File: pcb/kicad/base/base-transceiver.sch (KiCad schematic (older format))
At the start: 4 parts, among them U2 XBee-PRO_900HP

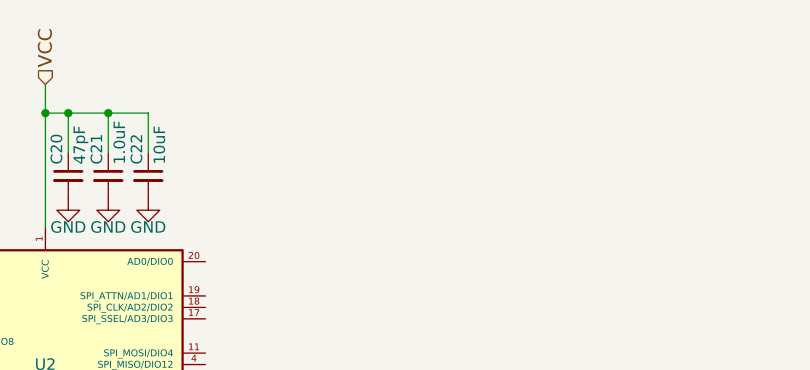
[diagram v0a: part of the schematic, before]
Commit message: Add initial layout for base daughterboard
Started the initial layout of the daughterboard with the
microcontroller. The inductors and crystals have placeholder footprints,
while the antenna and ferrite bead are TBD. Currently using default SMD
0402 size, but compact layout is still difficult to achieve. Crystals
have been placed as close as possible to the oscillator pins, but ground
return path is not optimized. Extent of components to be placed on
daughterboard still not finalized.
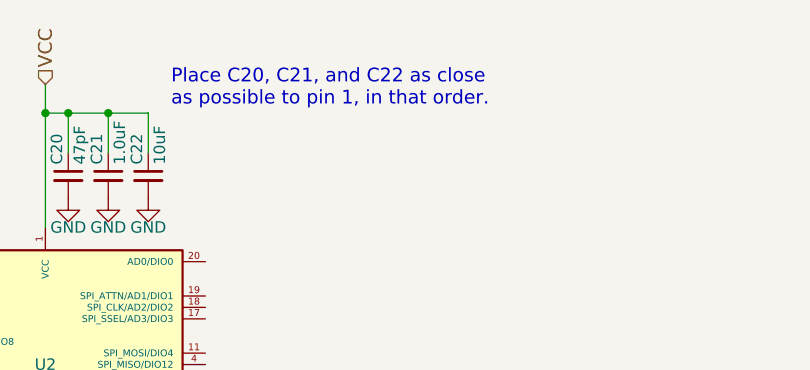
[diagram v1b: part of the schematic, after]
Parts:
- C20, C21, C22: footprint (none) -> Capacitors_SMD:C_0402
- U2: footprint Digi_XBee-PRO_TH -> RF_Modules:Digi_XBee-PRO_TH
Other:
- note added: "Place C20, C21, and C22 as close\nas possible to pin 1, in that order."
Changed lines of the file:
@@
 F 0 "U2" H 5850 3500 50  0000 C CNN
 F 1 "XBee-PRO_900HP" H 6300 2950 50  0000 C CNN
-F 2 "Digi_XBee-PRO_TH" H 6300 2875 50  0001 C CIN
+F 2 "RF_Modules:Digi_XBee-PRO_TH" H 6300 2875 50  0001 C CIN
 F 3 "" H 5850 3500 50  0000 C CNN
 	1    5850 3500
@@
 $EndComp
 $Comp
-L GND #PWR21
+L GND #PWR023
 U 1 1 58C1BBBE
 P 5850 4150
-F 0 "#PWR21" H 5850 3900 50  0001 C CNN
+F 0 "#PWR023" H 5850 3900 50  0001 C CNN
 F 1 "GND" H 5850 4000 50  0000 C CNN
 F 2 "" H 5850 4150 50  0000 C CNN
@@
 F 0 "C20" V 5900 2725 50  0000 L CNN
 F 1 "47pF" V 6000 2725 50  0000 L CNN
-F 2 "" H 5950 2675 50  0000 C CNN
+F 2 "Capacitors_SMD:C_0402" H 5950 2675 50  0001 C CNN
 F 3 "" H 5950 2675 50  0000 C CNN
 	1    5950 2675
@@
 $EndComp
 $Comp
-L GND #PWR22
+L GND #PWR024
 U 1 1 58C1C6E4
 P 5950 2775
-F 0 "#PWR22" H 5950 2525 50  0001 C CNN
+F 0 "#PWR024" H 5950 2525 50  0001 C CNN
 F 1 "GND" H 5950 2650 50  0000 C CNN
 F 2 "" H 5950 2775 50  0000 C CNN
@@
 F 0 "C21" V 6075 2725 50  0000 L CNN
 F 1 "1.0uF" V 6175 2725 50  0000 L CNN
-F 2 "" H 6125 2675 50  0000 C CNN
+F 2 "Capacitors_SMD:C_0402" H 6125 2675 50  0001 C CNN
 F 3 "" H 6125 2675 50  0000 C CNN
 	1    6125 2675
@@
 $EndComp
 $Comp
-L GND #PWR23
+L GND #PWR025
 U 1 1 58C1CE0A
 P 6125 2775
-F 0 "#PWR23" H 6125 2525 50  0001 C CNN
+F 0 "#PWR025" H 6125 2525 50  0001 C CNN
 F 1 "GND" H 6125 2650 50  0000 C CNN
 F 2 "" H 6125 2775 50  0000 C CNN
@@
 F 0 "C22" V 6250 2725 50  0000 L CNN
 F 1 "10uF" V 6350 2725 50  0000 L CNN
-F 2 "" H 6300 2675 50  0000 C CNN
+F 2 "Capacitors_SMD:C_0402" H 6300 2675 50  0001 C CNN
 F 3 "" H 6300 2675 50  0000 C CNN
 	1    6300 2675
@@
 $EndComp
 $Comp
-L GND #PWR24
+L GND #PWR026
 U 1 1 58C1CE37
 P 6300 2775
-F 0 "#PWR24" H 6300 2525 50  0001 C CNN
+F 0 "#PWR026" H 6300 2525 50  0001 C CNN
 F 1 "GND" H 6300 2650 50  0000 C CNN
 F 2 "" H 6300 2775 50  0000 C CNN
@@
 Text HLabel 5150 3800 0    30   Input ~ 0
 RTS
+Text Notes 6400 2375 0    60   ~ 0
+Place C20, C21, and C22 as close\nas possible to pin 1, in that order.
 $EndSCHEMATC

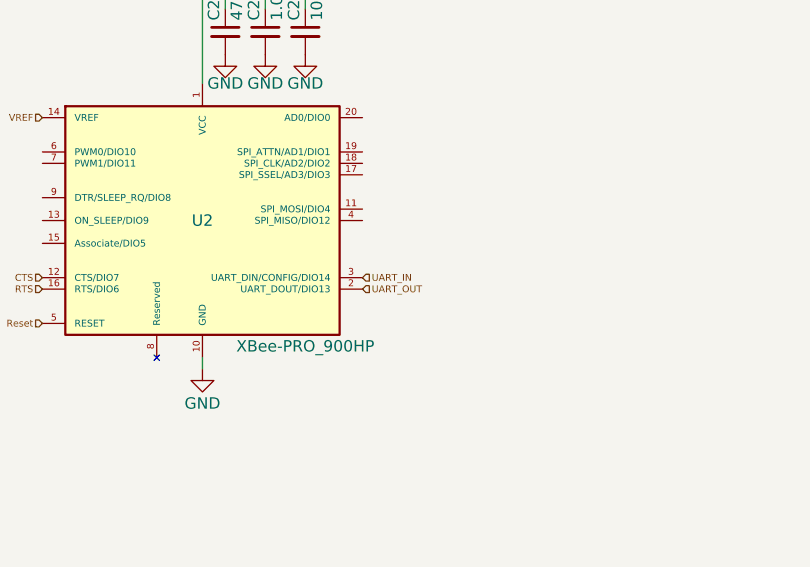
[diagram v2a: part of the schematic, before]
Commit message: Add more progress to crystal and XBee routing
Crystal has been moved to create a cleaner top layer for better signal
pathing. Daughterboard concept starting to be realized by adding vias
of pin header dimensions. Power routing still needs to be redone, and
and holes for ground header pins need to be placed.
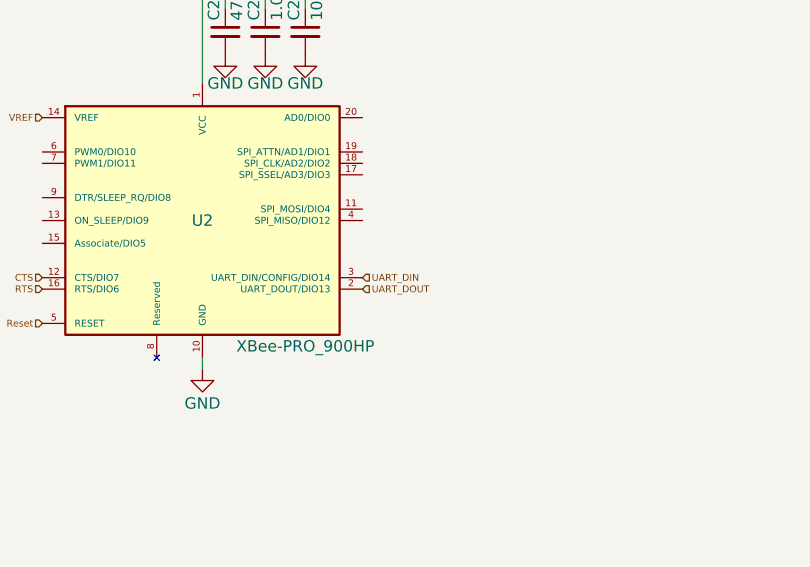
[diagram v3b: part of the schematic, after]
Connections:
- net UART_IN renamed UART_DIN
- net UART_OUT renamed UART_DOUT
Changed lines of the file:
@@
 Antenna needs to be connected\nthrough the on-chip SMA connector.
 Text HLabel 6550 3750 2    30   Input ~ 0
-UART_IN
+UART_DIN
 Text HLabel 6550 3800 2    30   Input ~ 0
-UART_OUT
+UART_DOUT
 Text HLabel 5150 3950 0    30   Input ~ 0
 Reset

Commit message: Cleanup base schematic and layout
Power routes have been placed to completely cover the entire board.
Crystal adjusted slightly to avoid the UART TX signal line. More vias
dispersed around the board for better ground connections. Gerber files
have been created and are ready to be tiled.
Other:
- note added: "0.1"
- note removed: "1.0"
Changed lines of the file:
@@
 EESchema Schematic File Version 2
-LIBS:base-rescue
 LIBS:power
 LIBS:device
@@
 March 4, 2017
 Text Notes 10600 7650 0    60   ~ 0
-1.0
+0.1
 $Comp
 L XBee-PRO_900HP U2
